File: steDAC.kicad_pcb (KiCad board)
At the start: 2 copper layers, 100 x 80 mm, 148 parts, among them IC10 TPS7A3001DGNT, IC11 ADP150AUJZ-3.3-R7, IC2 ES9038Q2M, IC3 ATSAMS70N20A-AN, IC4 ADP150AUJZ-3.3-R7, IC5 ADP150AUJZ-3.3-R7, IC6 ADP150AUJZ-3.3-R7, IC7 ADP150AUJZ-3.3-R7, IC8 LT1026CS8#PBF, IC9 ADP7118ARDZ, J2 USB4105-GF-A, J3 Conn_02x05_Odd_Even, J5 Conn_01x02, J6 Conn_01x04, J7 STX-3120-5B-284C, U2 OPA1612-Q1, U3 OPA1612-Q1, U4 OPA1622, Y2 SiT8209AI-21-33S-100.000000X, Y3 12MHz

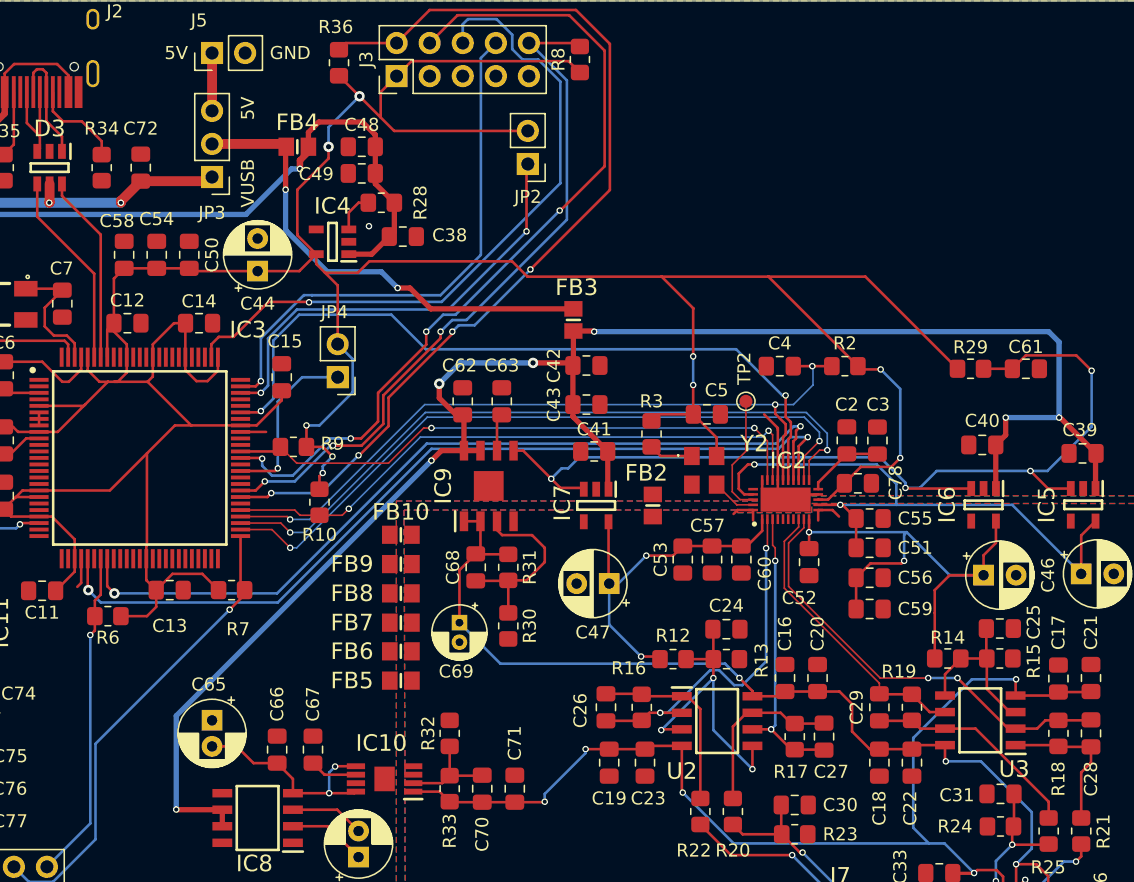
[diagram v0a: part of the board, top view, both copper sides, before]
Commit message: Adding part numbers for passives
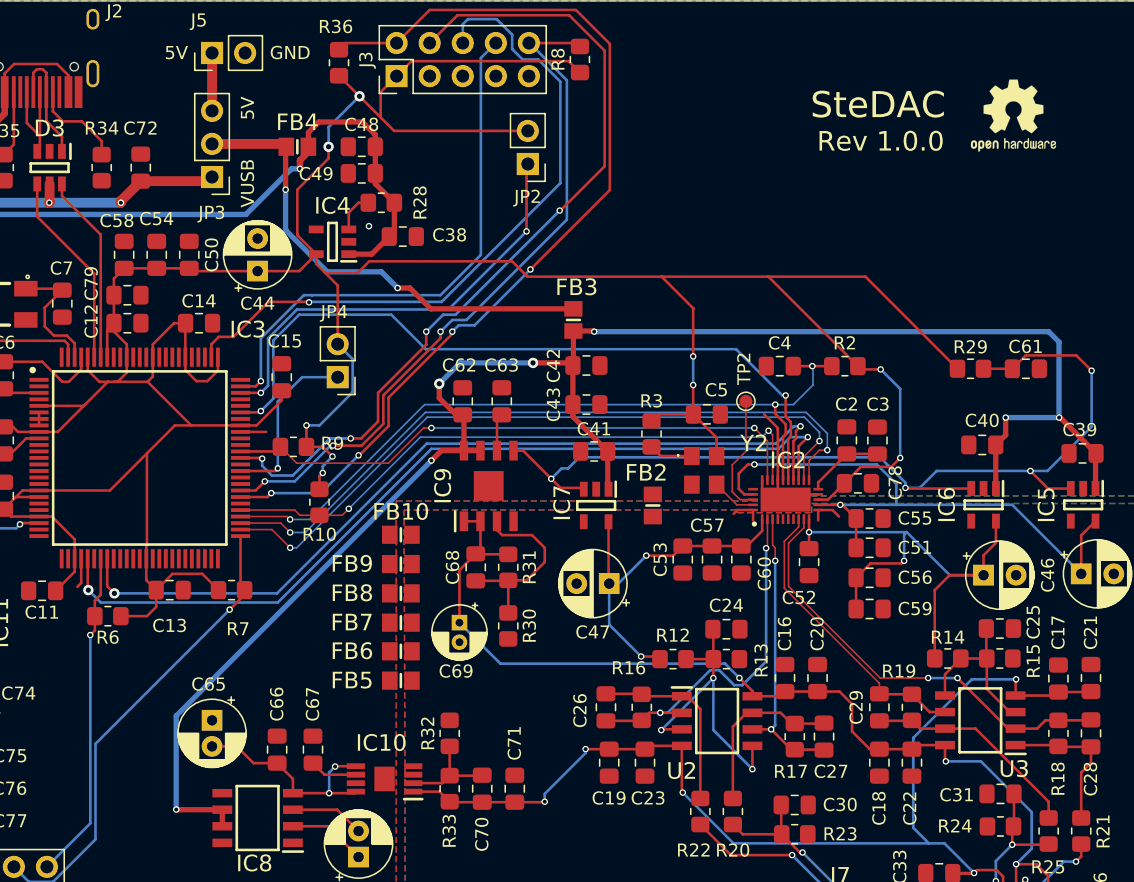
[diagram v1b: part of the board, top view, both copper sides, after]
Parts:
- added C79: 10u, Capacitor_SMD:C_0805_2012Metric_Pad1.18x1.45mm_HandSolder, F.Cu at (169.8, 92.6)
- added REF**: OSHW-Logo2_7.3x6mm_SilkScreen, Symbol:OSHW-Logo2_7.3x6mm_SilkScreen, F.Cu at (237.8, 78.8)
- C41: value C -> 4.7u
- R31: value 2.3k -> 23k
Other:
- board text added: "Rev 1.0.0"
- board text added: "SteDAC"

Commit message: Adding logos and finish up bom
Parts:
- added G***: LOGO, logo:crisis_boi, F.Cu at (205.8, 136.0)
- added G***: LOGO, logo:logo, F.Cu at (216.8, 81.6)
- moved REF** 2.84 mm to (240.0, 80.6)

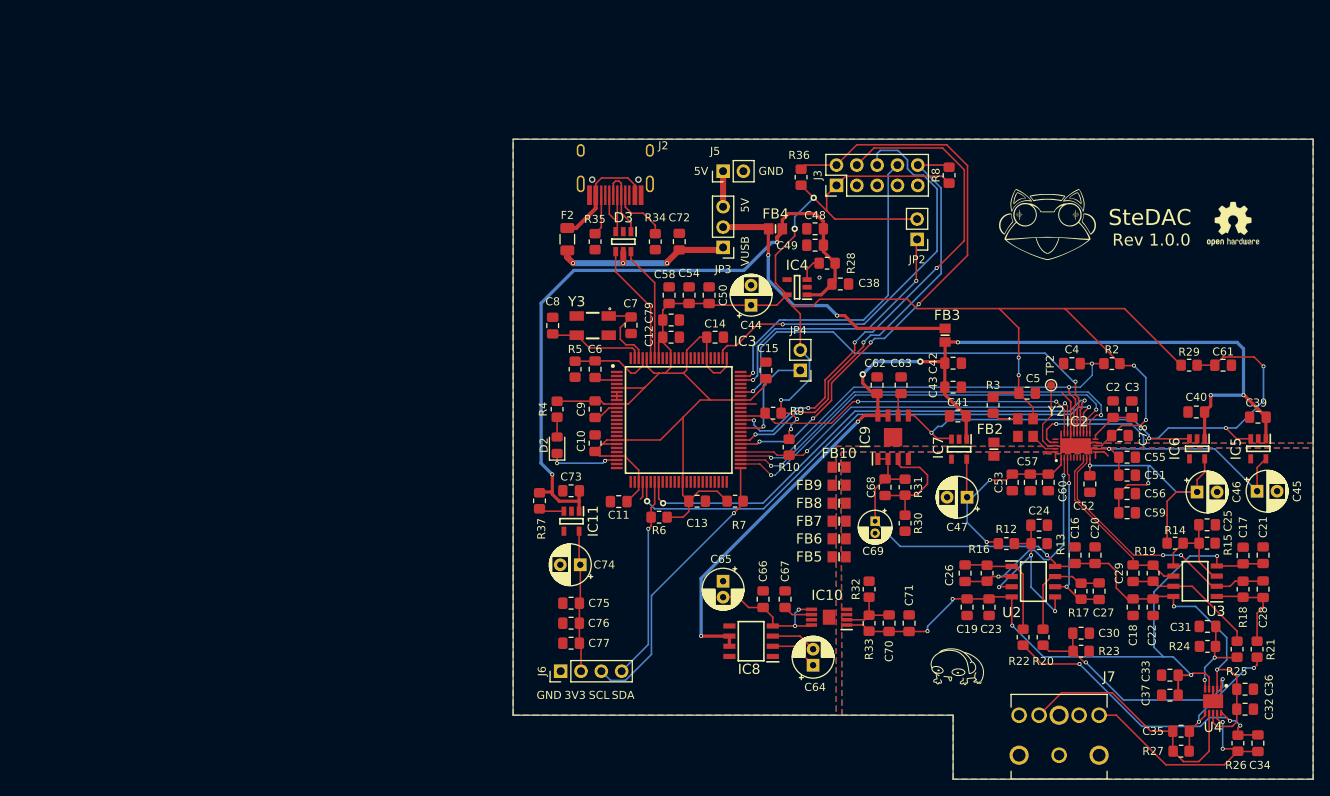
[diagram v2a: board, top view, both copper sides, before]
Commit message: Moving USB closer to edge. Adding silkscreen text for ERASE and JTAG_SEL. Updating README
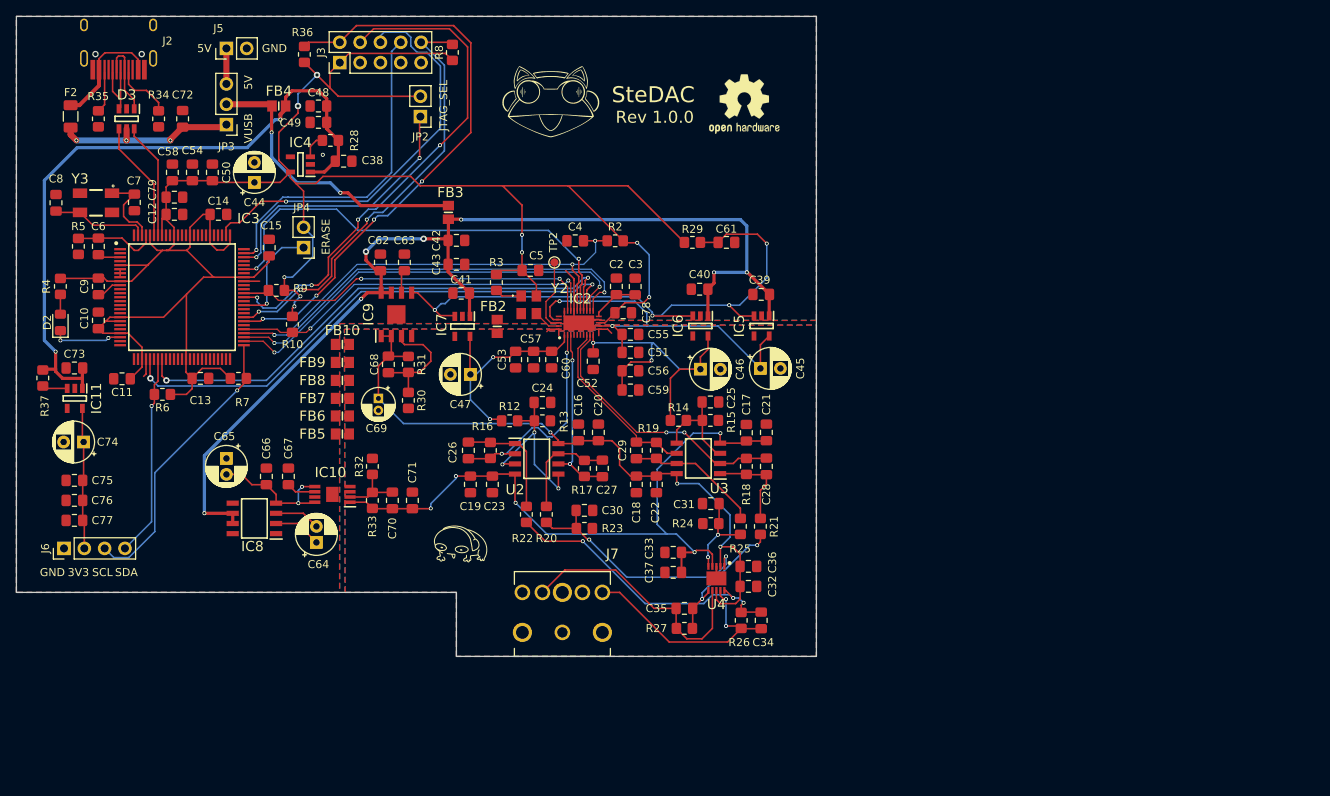
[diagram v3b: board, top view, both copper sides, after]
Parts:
- removed the REF** at (240.0, 80.6)
- added REF**: OSHW-Logo2_9.8x8mm_SilkScreen, Symbol:OSHW-Logo2_9.8x8mm_SilkScreen, F.Cu at (178.9, 65.6)
- moved J2 64.0 mm to (100.7, 53.1)
- moved C17 64.0 mm to (179.2, 106.7)
- moved C25 64.0 mm to (174.7, 102.8)
- moved C3 64.0 mm to (165.3, 88.4)
- moved C31 64.0 mm to (174.7, 115.5)
- moved C48 64.0 mm to (125.7, 65.8)
- moved C53 64.0 mm to (150.3, 97.5)
- moved C57 64.0 mm to (152.6, 97.5)
- moved C59 64.0 mm to (164.7, 101.3)
- moved C60 64.0 mm to (154.8, 97.5)
- moved C72 64.0 mm to (108.7, 67.5)
- moved C73 64.0 mm to (95.2, 98.6)
- moved C74 64.0 mm to (96.3, 107.8)
- moved D3 64.0 mm to (101.7, 67.5)
- moved FB4 64.0 mm to (120.7, 65.8)
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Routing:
- net JTAG_TDO: track 52.5 -> 51.6 mm
- net Net-(D3-Pad1): track 9.23 -> 9.91 mm
- net Net-(F2-Pad1): track 14.5 -> 15.1 mm
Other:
- board text added: "ERASE"
- board text added: "JTAG_SEL"
